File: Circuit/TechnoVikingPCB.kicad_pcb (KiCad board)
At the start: 2 copper layers, 76.9 x 53.5 mm, 127 parts, among them Q1 SQ4005EY-T1_BE3, Q2 BSS315PH6327XTSA1, Q3 BSS315PH6327XTSA1, Q4 BSS315PH6327XTSA1, U1 LMV324, U2 LMV324, X1 Conn_01x02_Male, X2 Conn_01x05_Male, X3 Conn_01x02_Male, X4 Conn_01x02_Male, X5 Conn_01x02_Female, X6 Conn_01x02_Male, X7 Conn_01x04_Male, X8 Conn_01x03_Male, X9 Conn_01x03_Male

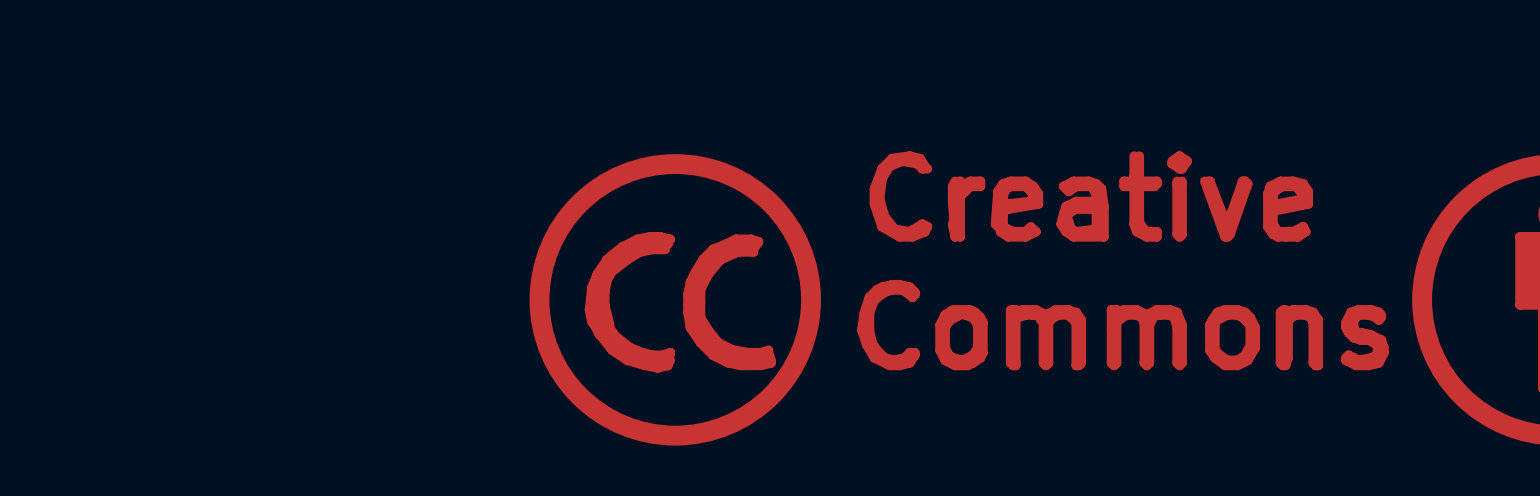
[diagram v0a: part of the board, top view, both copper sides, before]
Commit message: Assembly steps are finished.
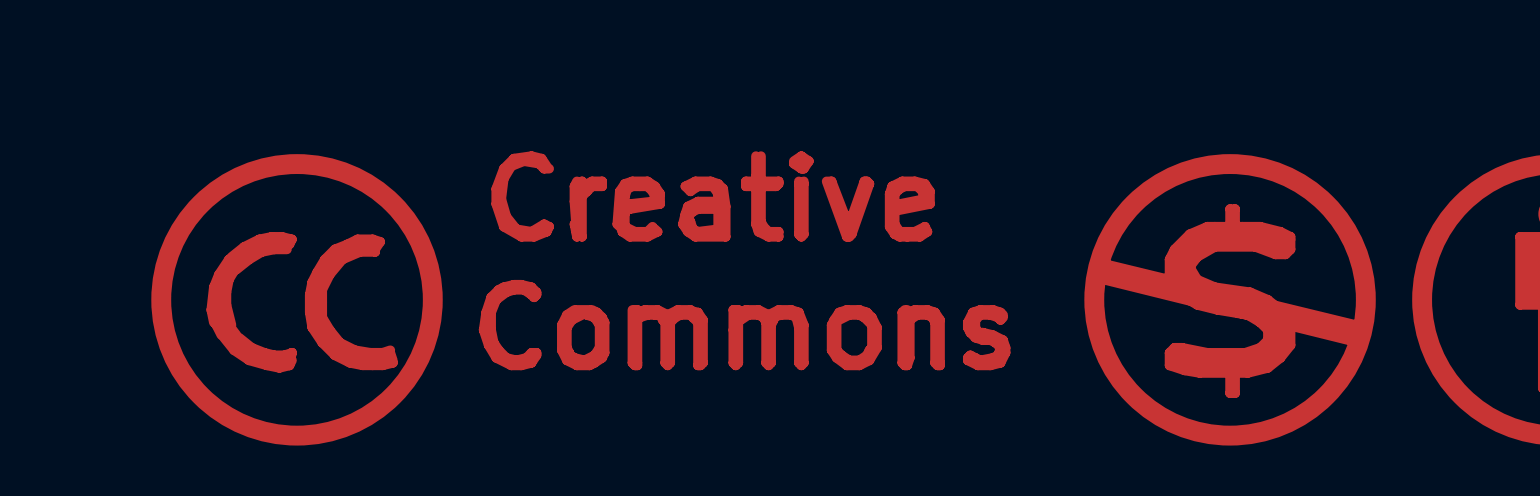
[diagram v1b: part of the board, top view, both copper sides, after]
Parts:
- added REF**: Symbol_CC-Noncommercial_CopperTop_Big, Symbol:Symbol_CC-Noncommercial_CopperTop_Big, F.Cu at (252.0, 174.0)
- moved REF** 15.0 mm to (215.0, 174.0)

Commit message: Documentation.
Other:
- board text added: "Techno Viking V1.0.1"
- board text removed: "Techno Viking V1.0"

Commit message: Documentation.
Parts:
- D4, D5, D9: value NSR0320MW2T1G -> PMEG4010BEA,115
- MK1: value Microphone_Condenser -> CMEJ-0627-42-P
- Q2, Q3, Q4: value BSS315PH6327XTSA1 -> BSH105,215
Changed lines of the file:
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@@
       (effects (font (size 1 1) (thickness 0.15)))
     )
-    (fp_text value "Microphone_Condenser" (at 0 3.8 -90 unlocked) (layer "F.Fab") hide
+    (fp_text value "CMEJ-0627-42-P" (at 0 3.8 -90 unlocked) (layer "F.Fab") hide
       (effects (font (size 1 1) (thickness 0.15)))
     )
@@
       (effects (font (size 1 1) (thickness 0.15)))
     )
-    (fp_text value "BSS315PH6327XTSA1" (at 0 2.4 90) (layer "F.Fab") hide
+    (fp_text value "BSH105,215" (at 0 2.4 90) (layer "F.Fab") hide
       (effects (font (size 1 1) (thickness 0.15)))
     )
@@
       (effects (font (size 1 1) (thickness 0.15)))
     )
-    (fp_text value "NSR0320MW2T1G" (at 0.1 1.9) (layer "F.Fab") hide
+    (fp_text value "PMEG4010BEA,115" (at 0.1 1.9) (layer "F.Fab") hide
       (effects (font (size 1 1) (thickness 0.15)))
     )
@@
       (effects (font (size 1 1) (thickness 0.15)))
     )
-    (fp_text value "NSR0320MW2T1G" (at 0.1 1.9 90) (layer "F.Fab") hide
+    (fp_text value "PMEG4010BEA,115" (at 0.1 1.9 90) (layer "F.Fab") hide
       (effects (font (size 1 1) (thickness 0.15)))
     )
@@
       (effects (font (size 1 1) (thickness 0.15)))
     )
-    (fp_text value "BSS315PH6327XTSA1" (at 2.9848 -0.3116 90) (layer "F.Fab") hide
+    (fp_text value "BSH105,215" (at 2.9848 -0.3116 90) (layer "F.Fab") hide
       (effects (font (size 1 1) (thickness 0.15)))
     )
@@
       (effects (font (size 1 1) (thickness 0.15)))
     )
-    (fp_text value "NSR0320MW2T1G" (at 0.1 1.9 90) (layer "F.Fab") hide
+    (fp_text value "PMEG4010BEA,115" (at 0.1 1.9 90) (layer "F.Fab") hide
       (effects (font (size 1 1) (thickness 0.15)))
     )
@@
       (effects (font (size 1 1) (thickness 0.15)))
     )
-    (fp_text value "BSS315PH6327XTSA1" (at 0 2.4 90) (layer "F.Fab") hide
+    (fp_text value "BSH105,215" (at 0 2.4 90) (layer "F.Fab") hide
       (effects (font (size 1 1) (thickness 0.15)))
     )
